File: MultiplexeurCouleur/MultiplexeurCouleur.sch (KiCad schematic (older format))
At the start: 28 parts, among them J1 Color0, J2 Color1, J3 Color2, J4 Color3, J5 Color4, J6 Color5, J7 Color6, J8 Color7, J9 Interf ARIG, U1 TCA9548APWR

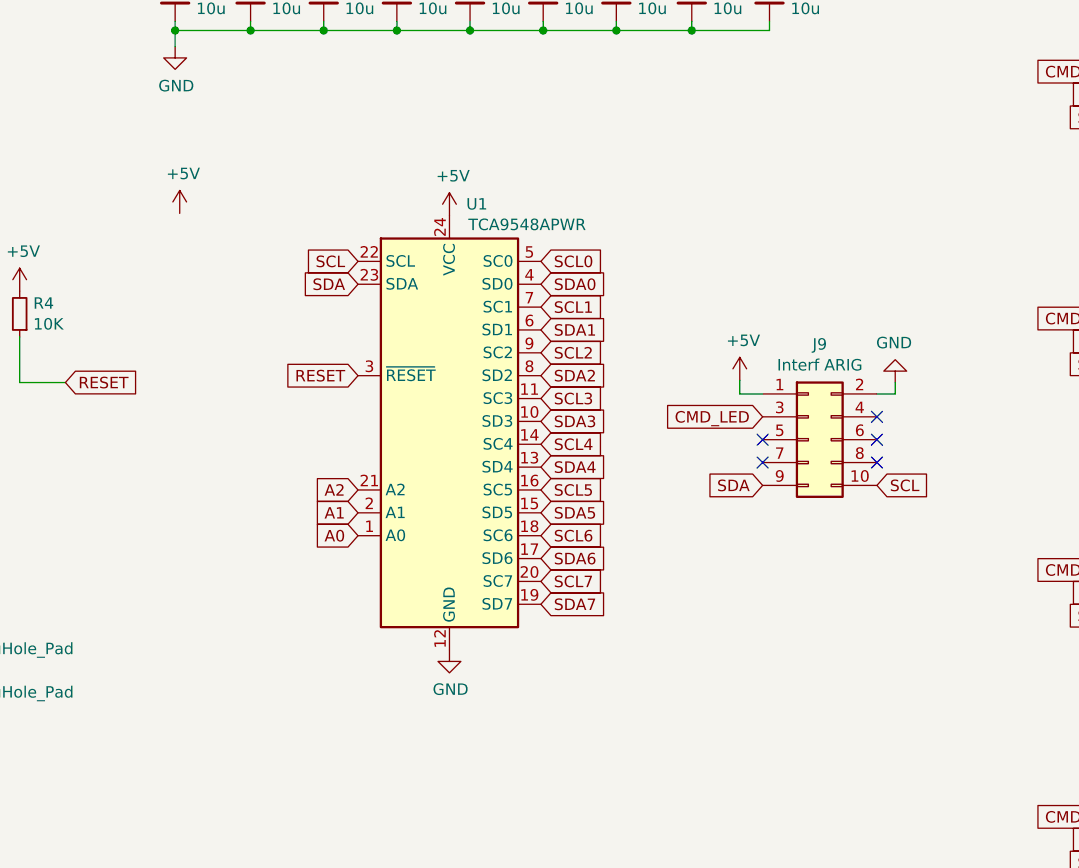
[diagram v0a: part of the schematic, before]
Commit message: Ajout bornier alim 5V sur multiplexeur couleur
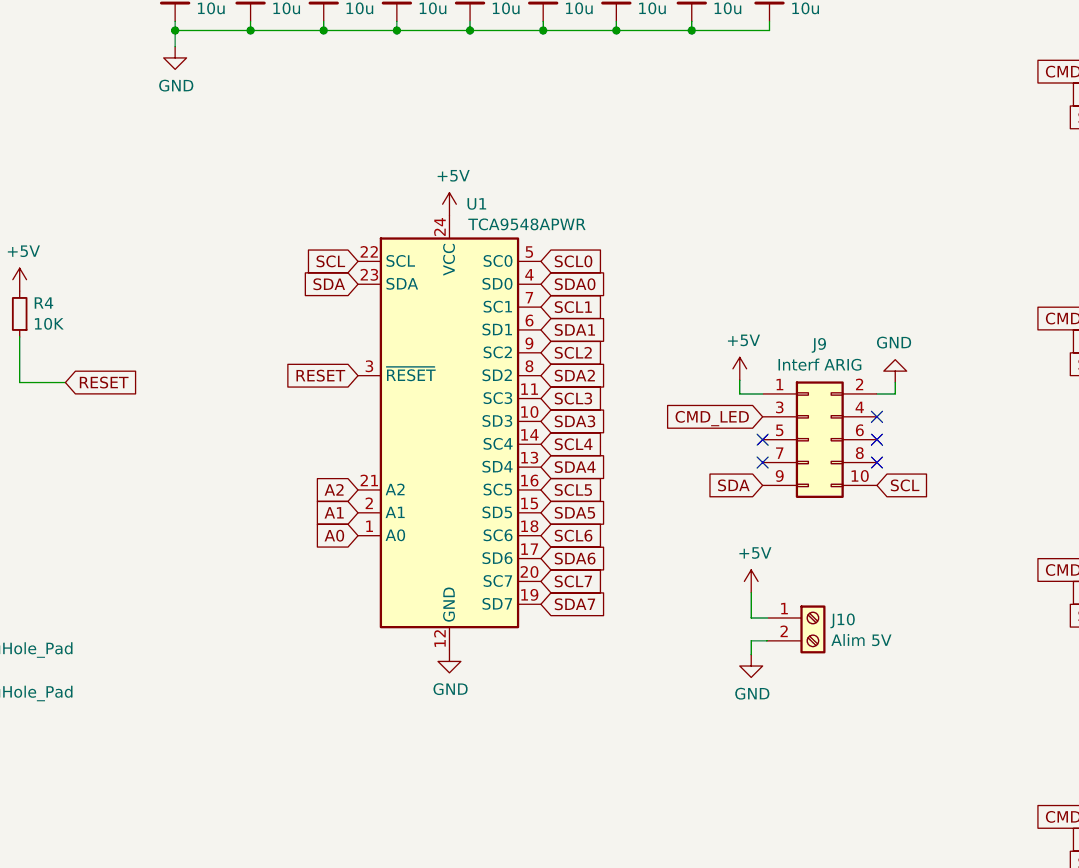
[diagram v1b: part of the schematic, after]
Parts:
- added J10: Alim 5V, TerminalBlock_Phoenix:TerminalBlock_Phoenix_MPT-0,5-2-2.54_1x02_P2.54mm_Horizontal, symbol Connector:Screw_Terminal_01x02
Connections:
- net +5V: now also J10.1 (Pin_1)
- net GND: now also J10.2 (Pin_2)
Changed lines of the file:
@@
 L power:+5V #PWR0101
 U 1 1 604116CF
-P 4000 2240
-F 0 "#PWR0101" H 4000 2090 50  0001 C CNN
-F 1 "+5V" H 4015 2413 50  0000 C CNN
-F 2 "" H 4000 2240 50  0001 C CNN
-F 3 "" H 4000 2240 50  0001 C CNN
-	1    4000 2240
+P 6500 3900
+F 0 "#PWR0101" H 6500 3750 50  0001 C CNN
+F 1 "+5V" H 6515 4073 50  0000 C CNN
+F 2 "" H 6500 3900 50  0001 C CNN
+F 3 "" H 6500 3900 50  0001 C CNN
+	1    6500 3900
 	1    0    0    -1
 $EndComp
@@
 	2560 4100 2560 4290
 Connection ~ 2560 4290
+$Comp
+L power:GND #PWR031
+U 1 1 606B28DF
+P 6500 4170
+F 0 "#PWR031" H 6500 3920 50  0001 C CNN
+F 1 "GND" H 6505 3997 50  0000 C CNN
+F 2 "" H 6500 4170 50  0001 C CNN
+F 3 "" H 6500 4170 50  0001 C CNN
+	1    6500 4170
+	1    0    0    -1
+$EndComp
+$Comp
+L Connector:Screw_Terminal_01x02 J10
+U 1 1 606B3858
+P 6770 4010
+F 0 "J10" H 6850 4002 50  0000 L CNN
+F 1 "Alim 5V" H 6850 3911 50  0000 L CNN
+F 2 "TerminalBlock_Phoenix:TerminalBlock_Phoenix_MPT-0,5-2-2.54_1x02_P2.54mm_Horizontal" H 6770 4010 50  0001 C CNN
+F 3 "~" H 6770 4010 50  0001 C CNN
+	1    6770 4010
+	1    0    0    -1
+$EndComp
+Wire Wire Line
+	6500 3900 6500 4010
+Wire Wire Line
+	6500 4010 6570 4010
+Wire Wire Line
+	6500 4170 6500 4110
+Wire Wire Line
+	6500 4110 6570 4110
 $EndSCHEMATC

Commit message: Finalisation multiplexeur couleur
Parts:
- C1, C2, C3, C4, C5, C6, C7, C8, C9: LCSC Part (none) -> C15850
- H1, H2, J1, J10, J2, J3, J4, J5, J6, J7, J8, J9, JP1, JP2, JP3: JLCPCB BOM (none) -> 0
- R1, R2, R3, R4: LCSC Part (none) -> C17414
- U1: LCSC Part (none) -> C130026
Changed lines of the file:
@@
 F 2 "Package_SO:TSSOP-24_4.4x7.8mm_P0.65mm" H 5180 2150 50  0001 C CNN
 F 3 "http://www.ti.com/lit/ds/symlink/tca9548a.pdf" H 5230 3400 50  0001 C CNN
+F 4 "C130026" H 5180 3150 50  0001 C CNN "LCSC Part"
 	1    5180 3150
 	1    0    0    -1
@@
 F 2 "Resistor_SMD:R_0805_2012Metric_Pad1.20x1.40mm_HandSolder" H 2750 3140 50  0001 C CNN
 F 3 "~" H 2750 3140 50  0001 C CNN
+F 4 "C17414" H 2750 3140 50  0001 C CNN "LCSC Part"
 	1    2750 3140
 	1    0    0    -1
@@
 F 2 "Resistor_SMD:R_0805_2012Metric_Pad1.20x1.40mm_HandSolder" H 2440 3140 50  0001 C CNN
 F 3 "~" H 2440 3140 50  0001 C CNN
+F 4 "C17414" H 2440 3140 50  0001 C CNN "LCSC Part"
 	1    2440 3140
 	1    0    0    -1
@@
 F 2 "Resistor_SMD:R_0805_2012Metric_Pad1.20x1.40mm_HandSolder" H 2110 3140 50  0001 C CNN
 F 3 "~" H 2110 3140 50  0001 C CNN
+F 4 "C17414" H 2110 3140 50  0001 C CNN "LCSC Part"
 	1    2110 3140
 	1    0    0    -1
@@
 F 2 "Jumper:SolderJumper-2_P1.3mm_Open_Pad1.0x1.5mm" H 2110 2740 50  0001 C CNN
 F 3 "~" H 2110 2740 50  0001 C CNN
+F 4 "0" H 2110 2740 50  0001 C CNN "JLCPCB BOM"
 	1    2110 2740
 	0    -1   -1   0
@@
 F 2 "Jumper:SolderJumper-2_P1.3mm_Open_Pad1.0x1.5mm" H 2440 2740 50  0001 C CNN
 F 3 "~" H 2440 2740 50  0001 C CNN
+F 4 "0" H 2440 2740 50  0001 C CNN "JLCPCB BOM"
 	1    2440 2740
 	0    -1   -1   0
@@
 F 2 "Jumper:SolderJumper-2_P1.3mm_Open_Pad1.0x1.5mm" H 2750 2740 50  0001 C CNN
 F 3 "~" H 2750 2740 50  0001 C CNN
+F 4 "0" H 2750 2740 50  0001 C CNN "JLCPCB BOM"
 	1    2750 2740
 	0    -1   -1   0
@@
 F 1 "10u" H 4072 1255 50  0000 L CNN
 F 2 "Capacitor_SMD:C_0805_2012Metric_Pad1.18x1.45mm_HandSolder" H 3980 1300 50  0001 C CNN
-F 3 "~" H 3980 1300 50  0001 C CNN
+F 3 "https://datasheet.lcsc.com/szlcsc/Samsung-Electro-Mechanics-CL21A106KAYNNNE_C15850.pdf" H 3980 1300 50  0001 C CNN
+F 4 "C15850" H 3980 1300 50  0001 C CNN "LCSC Part"
 	1    3980 1300
 	1    0    0    -1
@@
 F 2 "Resistor_SMD:R_0805_2012Metric_Pad1.20x1.40mm_HandSolder" H 3300 2680 50  0001 C CNN
 F 3 "~" H 3300 2680 50  0001 C CNN
+F 4 "C17414" H 3300 2680 50  0001 C CNN "LCSC Part"
 	1    3300 2680
 	-1   0    0    1
@@
 F 2 "Connector_IDC:IDC-Header_2x05_P2.54mm_Vertical" H 6750 3230 50  0001 C CNN
 F 3 "~" H 6750 3230 50  0001 C CNN
+F 4 "0" H 6750 3230 50  0001 C CNN "JLCPCB BOM"
 	1    6750 3230
 	1    0    0    -1
@@
 F 2 "Connector_JST:JST_PH_B5B-PH-K_1x05_P2.00mm_Vertical" H 8370 1720 50  0001 C CNN
 F 3 "~" H 8370 1720 50  0001 C CNN
+F 4 "0" H 8370 1720 50  0001 C CNN "JLCPCB BOM"
 	1    8370 1720
 	1    0    0    -1
@@
 F 2 "Connector_JST:JST_PH_B5B-PH-K_1x05_P2.00mm_Vertical" H 9590 1720 50  0001 C CNN
 F 3 "~" H 9590 1720 50  0001 C CNN
+F 4 "0" H 9590 1720 50  0001 C CNN "JLCPCB BOM"
 	1    9590 1720
 	1    0    0    -1
@@
 F 2 "Connector_JST:JST_PH_B5B-PH-K_1x05_P2.00mm_Vertical" H 8370 2800 50  0001 C CNN
 F 3 "~" H 8370 2800 50  0001 C CNN
+F 4 "0" H 8370 2800 50  0001 C CNN "JLCPCB BOM"
 	1    8370 2800
 	1    0    0    -1
@@
 F 2 "Connector_JST:JST_PH_B5B-PH-K_1x05_P2.00mm_Vertical" H 9590 2800 50  0001 C CNN
 F 3 "~" H 9590 2800 50  0001 C CNN
+F 4 "0" H 9590 2800 50  0001 C CNN "JLCPCB BOM"
 	1    9590 2800
 	1    0    0    -1
@@
 F 2 "Connector_JST:JST_PH_B5B-PH-K_1x05_P2.00mm_Vertical" H 8370 3900 50  0001 C CNN
 F 3 "~" H 8370 3900 50  0001 C CNN
+F 4 "0" H 8370 3900 50  0001 C CNN "JLCPCB BOM"
 	1    8370 3900
 	1    0    0    -1
@@
 F 2 "Connector_JST:JST_PH_B5B-PH-K_1x05_P2.00mm_Vertical" H 9590 3900 50  0001 C CNN
 F 3 "~" H 9590 3900 50  0001 C CNN
+F 4 "0" H 9590 3900 50  0001 C CNN "JLCPCB BOM"
 	1    9590 3900
 	1    0    0    -1
@@
 F 2 "Connector_JST:JST_PH_B5B-PH-K_1x05_P2.00mm_Vertical" H 8370 4980 50  0001 C CNN
 F 3 "~" H 8370 4980 50  0001 C CNN
+F 4 "0" H 8370 4980 50  0001 C CNN "JLCPCB BOM"
 	1    8370 4980
 	1    0    0    -1
@@
 F 2 "Connector_JST:JST_PH_B5B-PH-K_1x05_P2.00mm_Vertical" H 9590 4980 50  0001 C CNN
 F 3 "~" H 9590 4980 50  0001 C CNN
+F 4 "0" H 9590 4980 50  0001 C CNN "JLCPCB BOM"
 	1    9590 4980
 	1    0    0    -1
@@
 F 1 "10u" H 4402 1255 50  0000 L CNN
 F 2 "Capacitor_SMD:C_0805_2012Metric_Pad1.18x1.45mm_HandSolder" H 4310 1300 50  0001 C CNN
-F 3 "~" H 4310 1300 50  0001 C CNN
+F 3 "https://datasheet.lcsc.com/szlcsc/Samsung-Electro-Mechanics-CL21A106KAYNNNE_C15850.pdf" H 4310 1300 50  0001 C CNN
+F 4 "C15850" H 4310 1300 50  0001 C CNN "LCSC Part"
 	1    4310 1300
 	1    0    0    -1
@@
 F 1 "10u" H 4722 1255 50  0000 L CNN
 F 2 "Capacitor_SMD:C_0805_2012Metric_Pad1.18x1.45mm_HandSolder" H 4630 1300 50  0001 C CNN
-F 3 "~" H 4630 1300 50  0001 C CNN
+F 3 "https://datasheet.lcsc.com/szlcsc/Samsung-Electro-Mechanics-CL21A106KAYNNNE_C15850.pdf" H 4630 1300 50  0001 C CNN
+F 4 "C15850" H 4630 1300 50  0001 C CNN "LCSC Part"
 	1    4630 1300
 	1    0    0    -1
@@
 F 1 "10u" H 5042 1255 50  0000 L CNN
 F 2 "Capacitor_SMD:C_0805_2012Metric_Pad1.18x1.45mm_HandSolder" H 4950 1300 50  0001 C CNN
-F 3 "~" H 4950 1300 50  0001 C CNN
+F 3 "https://datasheet.lcsc.com/szlcsc/Samsung-Electro-Mechanics-CL21A106KAYNNNE_C15850.pdf" H 4950 1300 50  0001 C CNN
+F 4 "C15850" H 4950 1300 50  0001 C CNN "LCSC Part"
 	1    4950 1300
 	1    0    0    -1
@@
 F 1 "10u" H 5362 1255 50  0000 L CNN
 F 2 "Capacitor_SMD:C_0805_2012Metric_Pad1.18x1.45mm_HandSolder" H 5270 1300 50  0001 C CNN
-F 3 "~" H 5270 1300 50  0001 C CNN
+F 3 "https://datasheet.lcsc.com/szlcsc/Samsung-Electro-Mechanics-CL21A106KAYNNNE_C15850.pdf" H 5270 1300 50  0001 C CNN
+F 4 "C15850" H 5270 1300 50  0001 C CNN "LCSC Part"
 	1    5270 1300
 	1    0    0    -1
@@
 F 1 "10u" H 5682 1255 50  0000 L CNN
 F 2 "Capacitor_SMD:C_0805_2012Metric_Pad1.18x1.45mm_HandSolder" H 5590 1300 50  0001 C CNN
-F 3 "~" H 5590 1300 50  0001 C CNN
+F 3 "https://datasheet.lcsc.com/szlcsc/Samsung-Electro-Mechanics-CL21A106KAYNNNE_C15850.pdf" H 5590 1300 50  0001 C CNN
+F 4 "C15850" H 5590 1300 50  0001 C CNN "LCSC Part"
 	1    5590 1300
 	1    0    0    -1
@@
 F 1 "10u" H 6002 1255 50  0000 L CNN
 F 2 "Capacitor_SMD:C_0805_2012Metric_Pad1.18x1.45mm_HandSolder" H 5910 1300 50  0001 C CNN
-F 3 "~" H 5910 1300 50  0001 C CNN
+F 3 "https://datasheet.lcsc.com/szlcsc/Samsung-Electro-Mechanics-CL21A106KAYNNNE_C15850.pdf" H 5910 1300 50  0001 C CNN
+F 4 "C15850" H 5910 1300 50  0001 C CNN "LCSC Part"
 	1    5910 1300
 	1    0    0    -1
@@
 F 1 "10u" H 6332 1255 50  0000 L CNN
 F 2 "Capacitor_SMD:C_0805_2012Metric_Pad1.18x1.45mm_HandSolder" H 6240 1300 50  0001 C CNN
-F 3 "~" H 6240 1300 50  0001 C CNN
+F 3 "https://datasheet.lcsc.com/szlcsc/Samsung-Electro-Mechanics-CL21A106KAYNNNE_C15850.pdf" H 6240 1300 50  0001 C CNN
+F 4 "C15850" H 6240 1300 50  0001 C CNN "LCSC Part"
 	1    6240 1300
 	1    0    0    -1
@@
 F 1 "10u" H 6672 1255 50  0000 L CNN
 F 2 "Capacitor_SMD:C_0805_2012Metric_Pad1.18x1.45mm_HandSolder" H 6580 1300 50  0001 C CNN
-F 3 "~" H 6580 1300 50  0001 C CNN
+F 3 "https://datasheet.lcsc.com/szlcsc/Samsung-Electro-Mechanics-CL21A106KAYNNNE_C15850.pdf" H 6580 1300 50  0001 C CNN
+F 4 "C15850" H 6580 1300 50  0001 C CNN "LCSC Part"
 	1    6580 1300
 	1    0    0    -1
@@
 F 2 "MountingHole:MountingHole_3.2mm_M3_Pad_Via" H 2750 4100 50  0001 C CNN
 F 3 "~" H 2750 4100 50  0001 C CNN
+F 4 "0" H 2750 4100 50  0001 C CNN "JLCPCB BOM"
 	1    2750 4100
 	0    1    1    0
@@
 F 2 "MountingHole:MountingHole_3.2mm_M3_Pad_Via" H 2750 4290 50  0001 C CNN
 F 3 "~" H 2750 4290 50  0001 C CNN
+F 4 "0" H 2750 4290 50  0001 C CNN "JLCPCB BOM"
 	1    2750 4290
 	0    1    1    0
@@
 F 2 "TerminalBlock_Phoenix:TerminalBlock_Phoenix_MPT-0,5-2-2.54_1x02_P2.54mm_Horizontal" H 6770 4010 50  0001 C CNN
 F 3 "~" H 6770 4010 50  0001 C CNN
+F 4 "0" H 6770 4010 50  0001 C CNN "JLCPCB BOM"
 	1    6770 4010
 	1    0    0    -1
